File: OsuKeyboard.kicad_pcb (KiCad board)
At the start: 2 copper layers, 75 x 22 mm, 31 parts, among them J1 USB_B_Micro, J2 Conn_01x04_Female, SW1 SW_Push, SW2 SW_Push, SW3 RotaryEncoder_Switch, U1 STM32F401RBTx, U2 AMS1117-3.3, Y1 16MHz

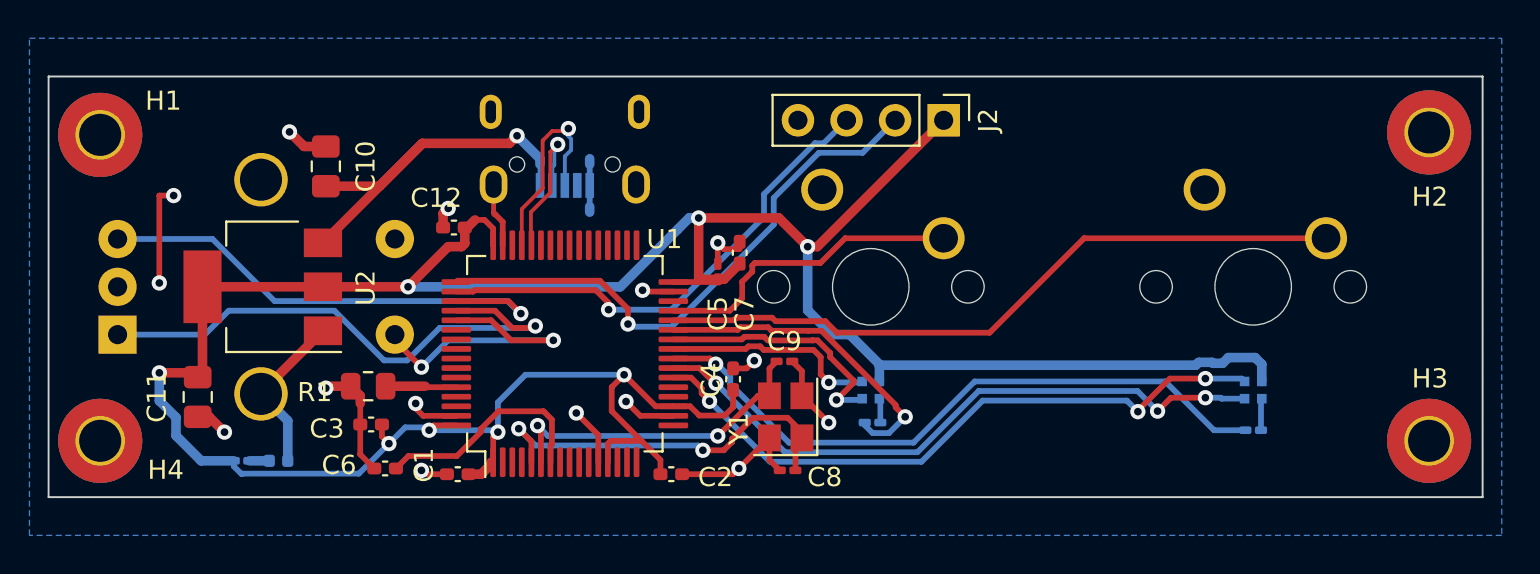
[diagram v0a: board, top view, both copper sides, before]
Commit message: Changed MCU and layout
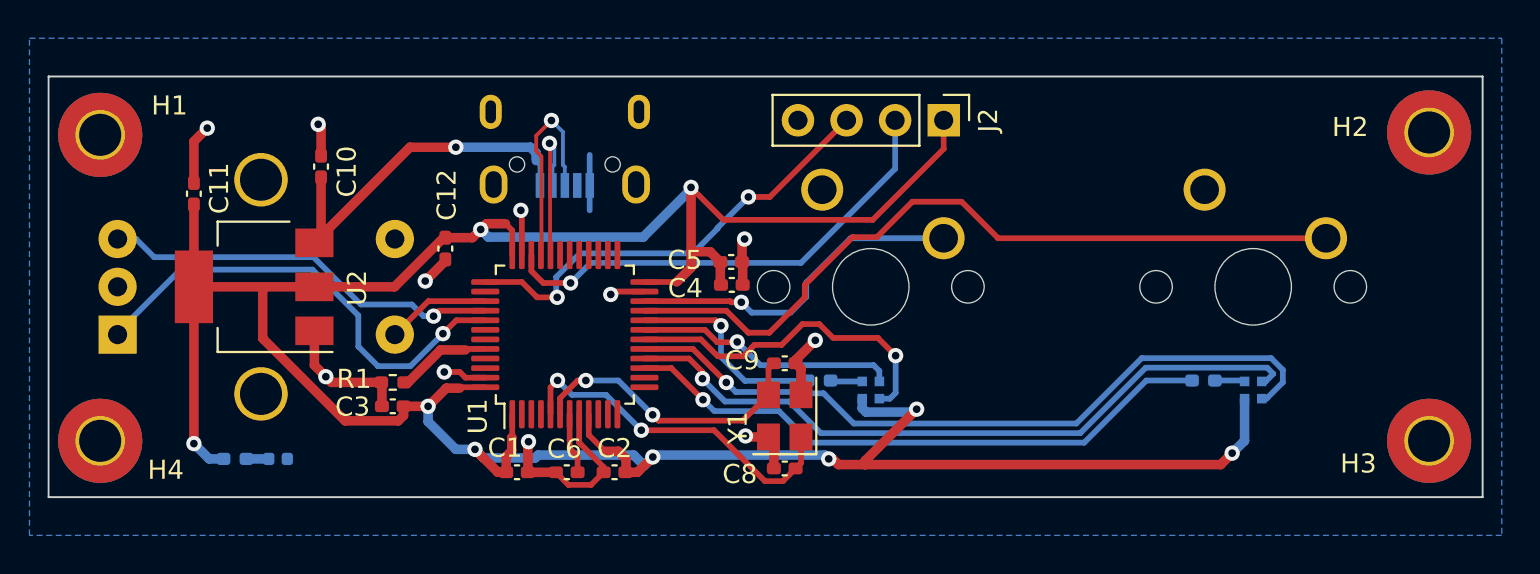
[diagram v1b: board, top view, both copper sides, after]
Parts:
- removed C7: 100n, Capacitor_SMD:C_0402_1005Metric_Pad0.74x0.62mm_HandSolder
- C10, C11: footprint Capacitor_SMD:C_0805_2012Metric_Pad1.18x1.45mm_HandSolder -> Capacitor_SMD:C_0402_1005Metric_Pad0.74x0.62mm_HandSolder
- C5, C8, C9: footprint Capacitor_SMD:C_0201_0603Metric_Pad0.64x0.40mm_HandSolder -> Capacitor_SMD:C_0402_1005Metric_Pad0.74x0.62mm_HandSolder
- R1: footprint Resistor_SMD:R_0805_2012Metric -> Resistor_SMD:R_0402_1005Metric_Pad0.72x0.64mm_HandSolder
- R2, R3, R4: footprint Resistor_SMD:R_0201_0603Metric_Pad0.64x0.40mm_HandSolder -> Resistor_SMD:R_0402_1005Metric_Pad0.72x0.64mm_HandSolder
- U1: value STM32F401RBTx -> STM32F103C6Tx; footprint Package_QFP:LQFP-64_10x10mm_P0.5mm -> Package_QFP:LQFP-48_7x7mm_P0.5mm
- moved C11 10.6 mm to (115.6, 109.6), turned to 90 degrees
- moved C6 9.50 mm to (135.1, 124.2)
- moved C4 4.93 mm to (143.7, 114.4), turned to 0 degrees
- moved R3 3.68 mm to (168.4, 119.4)
- moved R2 3.55 mm to (148.3, 119.4)
- moved C1 3.10 mm to (132.5, 124.2), turned to 0 degrees
- moved C2 2.97 mm to (137.6, 124.2), turned to 180 degrees
- moved C3 1.48 mm to (126.0, 120.8)
- moved R1 1.30 mm to (126.0, 119.5)
- moved C12 1.19 mm to (128.8, 112.5), turned to -90 degrees
- moved U1 1.00 mm to (135.0, 117.0)
- moved C5 0.86 mm to (143.7, 113.2), turned to 0 degrees
- moved U2 0.45 mm to (118.8, 114.5)
- moved R4 0.36 mm to (117.8, 123.5)
- moved C10 0.25 mm to (122.2, 108.2)
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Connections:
- SW3 pad A: /Rot_Encoder_A -> /rot_encoder_a
- SW3 pad B: /Rot_Encoder_B -> /rot_encoder_b
- SW3 pad S1: /Rot_Encoder_SW -> /rot_encoder_sw
- U1 pad 12: GND -> unconnected-(U1-Pad12)
- U1 pad 13: +3.3V -> unconnected-(U1-Pad13)
- U1 pad 15: unconnected-(U1-Pad15) -> /rgb2r
- U1 pad 16: unconnected-(U1-Pad16) -> /rgb2g
- U1 pad 17: unconnected-(U1-Pad17) -> /rgb2b
- U1 pad 18: GND -> /rgb1b
- U1 pad 19: +3.3V -> /rgb1g
- U1 pad 20: unconnected-(U1-Pad20) -> /rgb1r
- U1 pad 21: unconnected-(U1-Pad21) -> /sw2
- U1 pad 22: /rgb2b -> /sw1
- U1 pad 23: /rgb2g -> GND
- U1 pad 24: /rgb2r -> +3.3V
- U1 pad 25: /rgb1b -> unconnected-(U1-Pad25)
- U1 pad 26: /rgb1g -> unconnected-(U1-Pad26)
- U1 pad 27: /rgb1r -> unconnected-(U1-Pad27)
- U1 pad 28: /sw2 -> unconnected-(U1-Pad28)
- U1 pad 29: /sw1 -> unconnected-(U1-Pad29)
- U1 pad 31: GND -> unconnected-(U1-Pad31)
- U1 pad 32: +3.3V -> /usb-
- U1 pad 33: unconnected-(U1-Pad33) -> /usb+
- U1 pad 34: unconnected-(U1-Pad34) -> /swdio
- U1 pad 35: unconnected-(U1-Pad35) -> GND
- U1 pad 36: unconnected-(U1-Pad36) -> +3.3V
- U1 pad 37: unconnected-(U1-Pad37) -> /swclk
- U1 pad 39: unconnected-(U1-Pad39) -> /rot_encoder_sw
- U1 pad 40: unconnected-(U1-Pad40) -> /rot_encoder_b
- U1 pad 41: unconnected-(U1-Pad41) -> /rot_encoder_a
- U1 pad 44: /usb- -> /boot0
- U1 pad 45: /usb+ -> unconnected-(U1-Pad45)
- U1 pad 8: unconnected-(U1-Pad8) -> GND
- U1 pad 9: unconnected-(U1-Pad9) -> +3.3V
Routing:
- net /Rot_Encoder_A: track 28.7 -> 0.00 mm, vias 1 -> 0
- net /Rot_Encoder_B: track 26.4 -> 0.00 mm, vias 1 -> 0
- net /rot_encoder_a: track 0.00 -> 24.7 mm, vias 0 -> 1
- net /rot_encoder_b: track 0.00 -> 21.0 mm, vias 0 -> 1
- net GND: track 58.4 -> 41.4 mm, vias 15 -> 11
- net /Rot_Encoder_SW: track 15.4 -> 0.00 mm, vias 2 -> 0
- net /nrst: track 11.9 -> 3.21 mm
- net +3.3V: track 150.6 -> 157.4 mm, vias 8 -> 9
- net /rgb1b: track 11.3 -> 17.8 mm
- net /rgb1r: track 17.0 -> 10.8 mm
- net /rot_encoder_sw: track 0.00 -> 5.45 mm
- net /swdio: track 29.7 -> 25.1 mm
- net /rgb2b: track 34.2 -> 38.8 mm, vias 3 -> 1
- net /sw2: track 36.6 -> 40.1 mm
- net /rgb2g: track 33.8 -> 37.0 mm, vias 3 -> 1
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
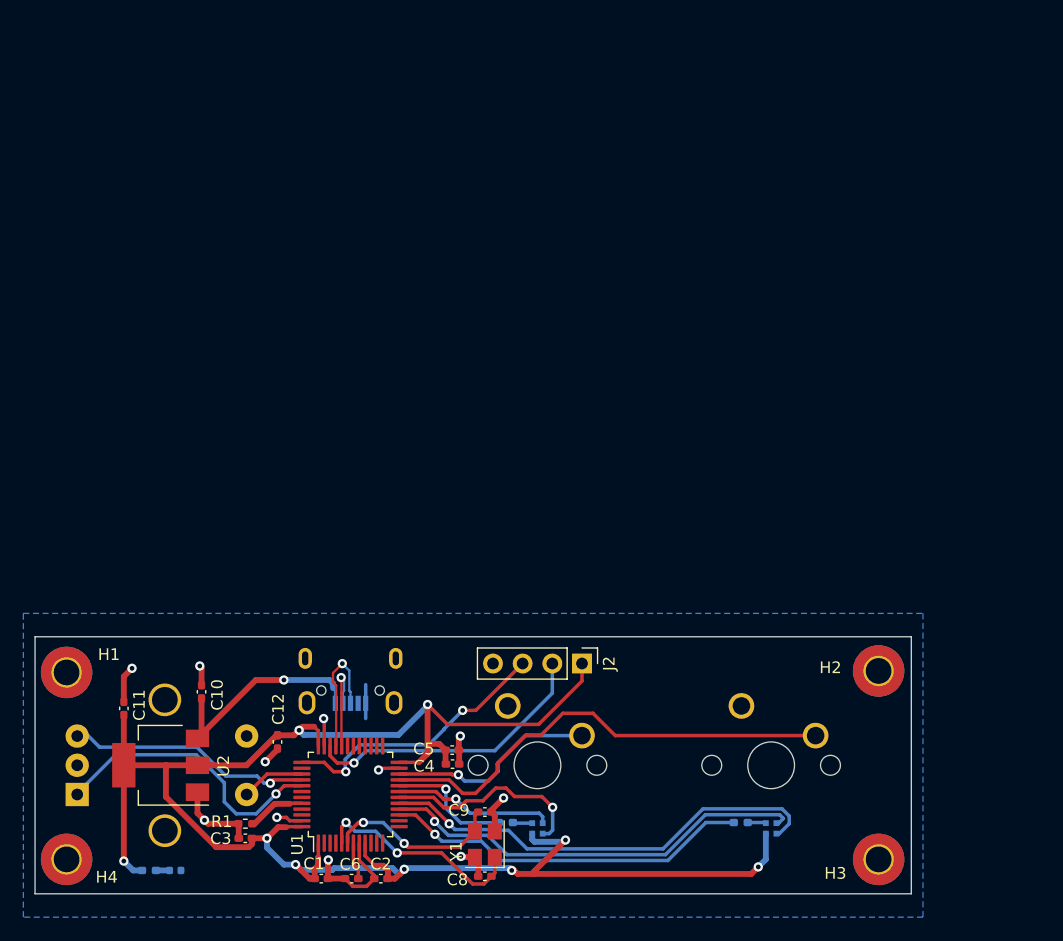
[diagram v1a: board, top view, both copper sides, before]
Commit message: simplified and made pcb smaller
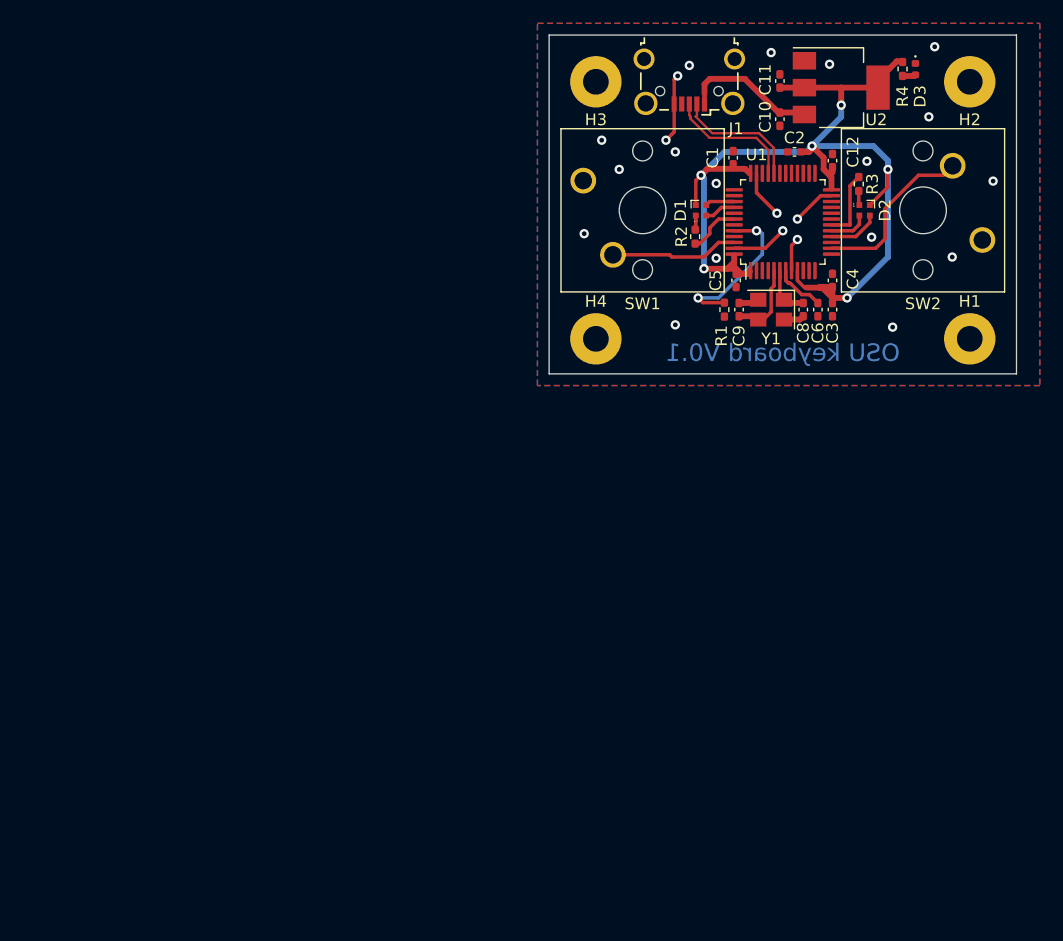
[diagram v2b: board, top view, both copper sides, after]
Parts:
- removed J2: Conn_01x04_Female, Connector_PinHeader_2.54mm:PinHeader_1x04_P2.54mm_Vertical
- removed SW3: RotaryEncoder_Switch, Rotary_Encoder:RotaryEncoder_Alps_EC12E-Switch_Vertical_H20mm_CircularMountingHoles
- D1, D2, D3, R2, R3, R4, SW1, SW2: moved to F.Cu
- H1, H2, H3, H4: footprint MountingHole:MountingHole_2.2mm_M2_Pad_TopBottom -> MountingHole:MountingHole_2.2mm_M2_Pad
- J1: footprint Connector_USB:USB_Micro-B_Wuerth_629105150521 -> Connector_USB:USB_Micro-B_Wuerth_629105150521_CircularHoles; moved to F.Cu
- moved R4 94.2 mm to (182.2, 54.9), turned to 90 degrees
- moved D3 93.4 mm to (183.3, 54.9), turned to -90 degrees
- moved H1 82.4 mm to (188.0, 78.0)
- moved U2 82.2 mm to (177.0, 56.5), turned to 0 degrees
- moved C11 77.7 mm to (171.8, 55.9)
- moved C2 71.6 mm to (173.0, 62.0)
- moved C1 71.1 mm to (167.8, 62.5), turned to 90 degrees
- moved H3 70.8 mm to (156.0, 56.0)
- moved C10 69.7 mm to (171.8, 59.2), turned to -90 degrees
- moved C12 68.8 mm to (176.2, 62.8), turned to 90 degrees
- moved C3 67.6 mm to (176.2, 75.5), turned to -90 degrees
- moved H4 63.5 mm to (156.0, 78.0)
- moved C6 63.0 mm to (175.0, 75.5), turned to 90 degrees
- moved U1 61.4 mm to (172.0, 68.0)
- moved R1 60.1 mm to (167.0, 75.5), turned to -90 degrees
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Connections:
- U1 pad 14: unconnected-(U1-Pad14) -> /sw2
- U1 pad 15: /rgb2r -> unconnected-(U1-Pad15)
- U1 pad 16: /rgb2g -> /rgb2b
- U1 pad 17: /rgb2b -> /rgb2g
- U1 pad 18: /rgb1b -> /rgb2r
- U1 pad 19: /rgb1g -> unconnected-(U1-Pad19)
- U1 pad 20: /rgb1r -> unconnected-(U1-Pad20)
- U1 pad 21: /sw2 -> unconnected-(U1-Pad21)
- U1 pad 22: /sw1 -> unconnected-(U1-Pad22)
- U1 pad 34: /swdio -> unconnected-(U1-Pad34)
- U1 pad 37: /swclk -> unconnected-(U1-Pad37)
- U1 pad 39: /rot_encoder_sw -> /rgb1b
- U1 pad 40: /rot_encoder_b -> /rgb1g
- U1 pad 41: /rot_encoder_a -> unconnected-(U1-Pad41)
- U1 pad 42: unconnected-(U1-Pad42) -> /rgb1r
- U1 pad 46: unconnected-(U1-Pad46) -> /sw1
- U1 pad 5: /osc_in -> /osc_out
- U1 pad 6: /osc_out -> /osc_in
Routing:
- net +3.3V: track 157.4 -> 89.3 mm, vias 9 -> 6
- net /rgb2b: track 38.8 -> 4.38 mm, vias 1 -> 0
- net /rgb2g: track 37.0 -> 3.37 mm, vias 1 -> 0
- net /rgb2r: track 31.6 -> 6.00 mm, vias 1 -> 0
- net /sw2: track 40.1 -> 14.8 mm
- net /swdio: track 25.1 -> 0.00 mm, vias 1 -> 0
- net /rot_encoder_a: track 24.7 -> 0.00 mm, vias 1 -> 0
- net /swclk: track 23.8 -> 0.00 mm, vias 2 -> 0
- net /rot_encoder_b: track 21.0 -> 0.00 mm, vias 1 -> 0
- net GND: track 41.4 -> 25.0 mm, vias 11 -> 23
- net /rgb1b: track 17.8 -> 2.51 mm, vias 1 -> 0
- net /osc_in: track 18.6 -> 4.40 mm, vias 2 -> 0
- net /rgb1g: track 13.7 -> 2.68 mm, vias 1 -> 0
- net /boot0: track 4.96 -> 13.8 mm, vias 0 -> 2
- net /osc_out: track 15.3 -> 6.78 mm, vias 2 -> 0
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- added copper zone on F.Cu, net GND
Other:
- board size 75 x 22 mm -> 40 x 29 mm
- board text added: "Brasil 2022"
- board text added: "OSU keyboard V0.1"
- board text added: "OSU keypad V0.1"
- board text added: "OwO oWo OwO oWo"
